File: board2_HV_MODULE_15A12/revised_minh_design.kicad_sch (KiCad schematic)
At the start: 18 parts, among them J1 Conn_01x07_Male, J2 Conn_01x01_Male, U1 LM7805_TO220, U2 NE5532, U4 15A12

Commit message: JLCPCB Submission for 15A12 board
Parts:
- U4: footprint Converter_DCDC:Advanced Energy 15A12P4 -> Library:Advanced Energy 15A12P4
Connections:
- net DAC_SIG: now also J1.6 (Pin_6); no longer J1.3 (Pin_3)
- net Earth: no longer J1.7 (Pin_7)
- net VPGM: now also J1.7 (Pin_7); no longer J1.6 (Pin_6)
- net ENABLE: now reaches U4.4 (HV_ENABLE)
- net ENABLE: now also J1.3 (Pin_3)
- no-connect marks 5 -> 4
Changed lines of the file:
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@@
   (junction (at 175.26 66.04) (diameter 0) (color 0 0 0 0)
   )
-  (no_connect (at 205.74 69.85))
   (no_connect (at 233.68 92.71))
   (no_connect (at 105.41 27.94))
@@
     (effects (font (size 1.27 1.27)) (justify left bottom))
   )
+  (global_label "ENABLE" (shape input) (at 49.53 33.02 0) (fields_autoplaced)
+    (effects (font (size 1.27 1.27)) (justify left))
+    (property "Intersheet References" "${INTERSHEET_REFS}" (id 0) (at 58.9583 32.9406 0)
+      (effects (font (size 1.27 1.27)) (justify left) hide)
+    )
+  )
+  (global_label "DAC_SIG" (shape input) (at 49.53 40.64 0) (fields_autoplaced)
+    (effects (font (size 1.016 1.016)) (justify left))
+    (property "Intersheet References" "${INTERSHEET_REFS}" (id 0) (at 57.6048 40.5765 0)
+      (effects (font (size 1.016 1.016)) (justify left) hide)
+    )
+  )
   (global_label "VMON_3V3" (shape input) (at 111.76 102.87 180) (fields_autoplaced)
     (effects (font (size 1.016 1.016)) (justify right))
@@
     )
   )
+  (global_label "VPGM" (shape input) (at 49.53 43.18 0) (fields_autoplaced)
+    (effects (font (size 1.016 1.016)) (justify left))
+    (property "Intersheet References" "${INTERSHEET_REFS}" (id 0) (at 55.5244 43.2435 0)
+      (effects (font (size 1.016 1.016)) (justify left) hide)
+    )
+  )
   (global_label "DAC_SIG" (shape input) (at 105.41 50.8 180) (fields_autoplaced)
     (effects (font (size 1.016 1.016)) (justify right))
@@
     )
   )
+  (global_label "ENABLE" (shape input) (at 205.74 69.85 180) (fields_autoplaced)
+    (effects (font (size 1.27 1.27)) (justify right))
+    (property "Intersheet References" "${INTERSHEET_REFS}" (id 0) (at 196.3117 69.9294 0)
+      (effects (font (size 1.27 1.27)) (justify right) hide)
+    )
+  )
   (global_label "VMON" (shape input) (at 173.99 62.23 180) (fields_autoplaced)
     (effects (font (size 1.016 1.016)) (justify right))
@@
     )
   )
-  (global_label "SGND" (shape input) (at 49.53 43.18 0) (fields_autoplaced)
-    (effects (font (size 1.27 1.27)) (justify left))
-    (property "Intersheet References" "${INTERSHEET_REFS}" (id 0) (at 57.0231 43.1006 0)
-      (effects (font (size 1.27 1.27)) (justify left) hide)
-    )
-  )
   (global_label "SGND" (shape input) (at 104.14 71.12 180) (fields_autoplaced)
     (effects (font (size 1.27 1.27)) (justify right))
@@
     )
   )
-  (global_label "DAC_SIG" (shape input) (at 49.53 33.02 0) (fields_autoplaced)
-    (effects (font (size 1.016 1.016)) (justify left))
-    (property "Intersheet References" "${INTERSHEET_REFS}" (id 0) (at 57.6048 32.9565 0)
-      (effects (font (size 1.016 1.016)) (justify left) hide)
-    )
-  )
   (global_label "SGND" (shape input) (at 114.3 114.3 270) (fields_autoplaced)
     (effects (font (size 1.27 1.27)) (justify right))
@@
     (property "Intersheet References" "${INTERSHEET_REFS}" (id 0) (at 133.4294 121.7931 90)
       (effects (font (size 1.27 1.27)) (justify right) hide)
-    )
-  )
-  (global_label "VPGM" (shape input) (at 49.53 40.64 0) (fields_autoplaced)
-    (effects (font (size 1.016 1.016)) (justify left))
-    (property "Intersheet References" "${INTERSHEET_REFS}" (id 0) (at 55.5244 40.7035 0)
-      (effects (font (size 1.016 1.016)) (justify left) hide)
     )
   )
@@
       (effects (font (size 1.27 1.27)) (justify left))
     )
-    (property "Footprint" "Converter_DCDC:Advanced Energy 15A12P4" (id 2) (at 205.74 60.96 0)
+    (property "Footprint" "Library:Advanced Energy 15A12P4" (id 2) (at 205.74 60.96 0)
       (effects (font (size 1.27 1.27)) hide)
     )
@@
     )
     (path "/e586f466-4d6e-44b1-a629-a3003ee0dde8"
-      (reference "U4") (unit 1) (value "15A12") (footprint "Converter_DCDC:Advanced Energy 15A12P4")
-    )
-  )
+      (reference "U4") (unit 1) (value "15A12") (footprint "Library:Advanced Energy 15A12P4")
+    )
+  )

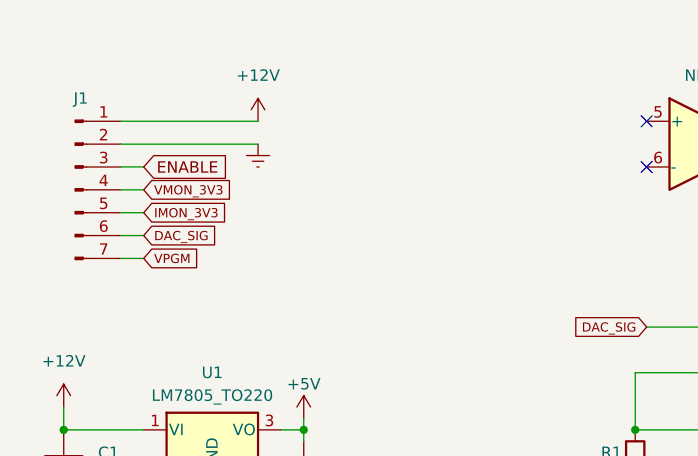
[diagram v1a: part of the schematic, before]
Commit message: JLCPCB Submission for 15A12 board, double row connectors added, separate power and signal connectors
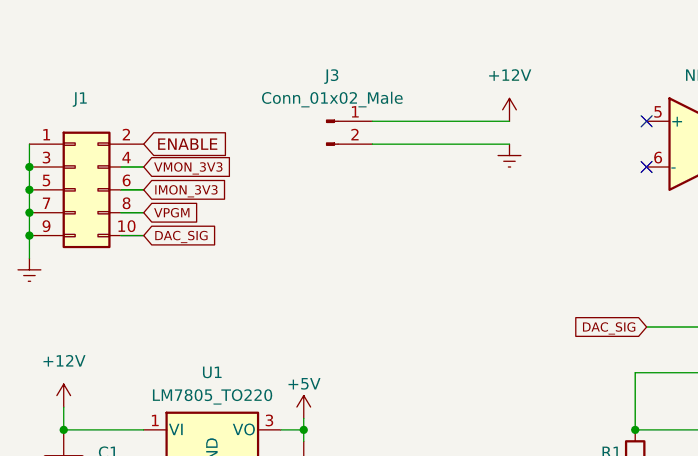
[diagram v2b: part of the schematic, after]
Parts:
- added J3: Conn_01x02_Male, Connector_PinSocket_2.54mm:PinSocket_1x02_P2.54mm_Vertical, symbol Connector:Conn_01x02_Male
- J1: footprint Connector_PinSocket_2.54mm:PinSocket_1x07_P2.54mm_Vertical -> Connector_PinSocket_2.54mm:PinSocket_2x05_P2.54mm_Vertical; symbol Connector:Conn_01x07_Male -> Connector_Generic:Conn_02x05_Odd_Even
- R4: footprint Resistor_THT:R_Axial_DIN0207_L6.3mm_D2.5mm_P10.16mm_Horizontal -> Resistor_THT:R_Axial_DIN0207_L6.3mm_D2.5mm_P7.62mm_Horizontal
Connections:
- net +12V: now also J3.1 (Pin_1); no longer J1.1 (Pin_1)
- net DAC_SIG: now also J1.10 (Pin_10); no longer J1.6 (Pin_6)
- net ENABLE: now also J1.2 (Pin_2); no longer J1.3 (Pin_3)
- net Earth: now also J1.1 (Pin_1), J1.3 (Pin_3), J1.5 (Pin_5), J1.7 (Pin_7), J1.9 (Pin_9), J3.2 (Pin_2); no longer J1.2 (Pin_2)
- net IMON_3V3: now also J1.6 (Pin_6); no longer J1.5 (Pin_5)
- net VPGM: now also J1.8 (Pin_8); no longer J1.7 (Pin_7)

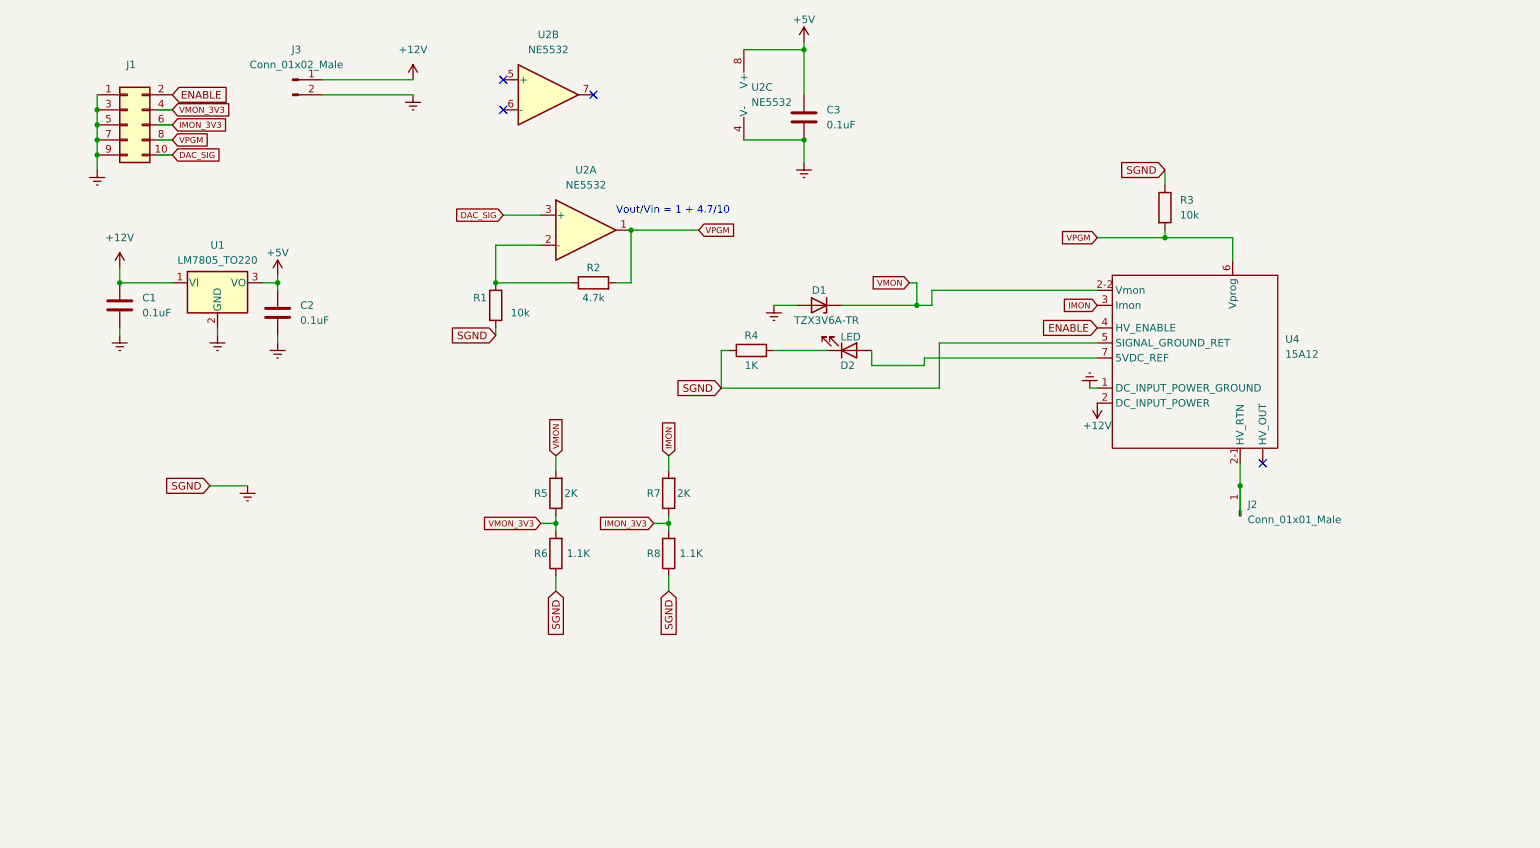
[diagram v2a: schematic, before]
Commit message: exported STEP file. Minor changes to schematics for better documentations
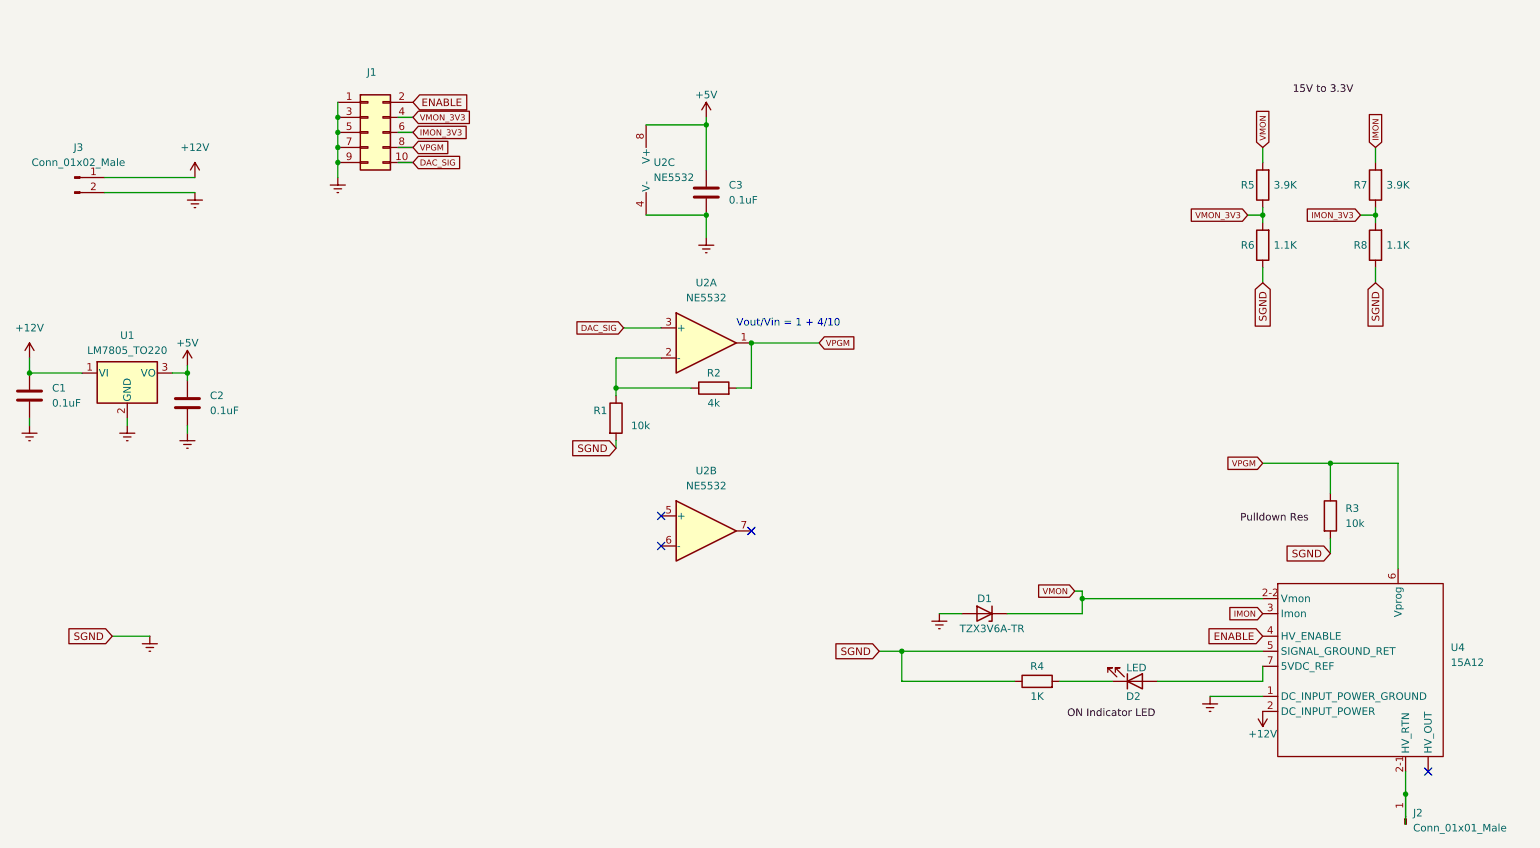
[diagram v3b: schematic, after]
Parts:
- J2: now left out of the parts list
- R2: value 4.7k -> 4k
- R5, R7: value 2K -> 3.9K
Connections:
- net Earth: now also R3.2; no longer R3.1
- net VPGM: now also R3.1; no longer R3.2
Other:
- note added: "Vout/Vin = 1 + 4/10"
- note removed: "Vout/Vin = 1 + 4.7/10"
- moved on the sheet: C1, C2, C3, D1, D2, J1, J2, J3, R1, R2, R3, R4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
